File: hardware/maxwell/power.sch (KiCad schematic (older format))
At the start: 30 parts

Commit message: Adding finalized PCB layout.
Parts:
- removed C?: 100u, symbol CP
- added C17, C21: 15, fruchti/fruchtilib/mod/rcl.pretty:CP_13mm_200, symbol CP
- C15: renamed from C?; value ?500u -> 100u; footprint (none) -> xesscorp/xess.pretty:xess-ECAP-SMT-6.3MM
- C16, C18, C20: renamed from C?; footprint (none) -> coddingtonbear/coddingtonbear.pretty:0805_Milling
- C19: renamed from C?; value ?500u -> 220u; footprint (none) -> xesscorp/xess.pretty:xess-ECAP-SMT-6.3MM
- D1, D5, D6: renamed from D?; footprint (none) -> mcous/kicad-lib/footprints/diode.pretty:DO-214AC
- D2, D3: renamed from D?; value 25V -> 20; footprint (none) -> Tinkerforge/kicad-libraries:SOD523
- D4: renamed from D?; footprint (none) -> ep092/library_toni.pretty:SO-4
- J7, J9: renamed from J?; footprint (none) -> ChristianLerche/LercheTech_KiCAD/LercheTech.pretty:Lerche_2P_2.54mm_Terminal
- J8: renamed from J?; footprint (none) -> coddingtonbear/coddingtonbear.pretty:UJ2-MIBH-4-SMT
- R14, R15, R16, R17, R18, R19, R20, R21, R22, R23, R24: renamed from R?; footprint (none) -> coddingtonbear/coddingtonbear.pretty:0805_Milling
- U*1: renamed from U*?; footprint (none) -> apexelectrix/apex-smd.pretty:SOT-23-5
- U10: renamed from U?; footprint TO_SOT_Packages_THT:TO-220-4_Vertical -> KiCad/TO_SOT_Packages_THT.pretty:TO-220-5_Pentawatt_Multiwatt-5_Horizontal_StaggeredType2
- U8: renamed from U?; footprint Housings_SSOP:MFSOP6-4_4.4x3.6mm_Pitch1.27mm -> Tinkerforge/kicad-libraries:SO-4
- U9: renamed from U?; footprint (none) -> coddingtonbear/coddingtonbear.pretty:BOOST_LM2596_3A
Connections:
- net labels removed: Earth
- wire segments 60 -> 63

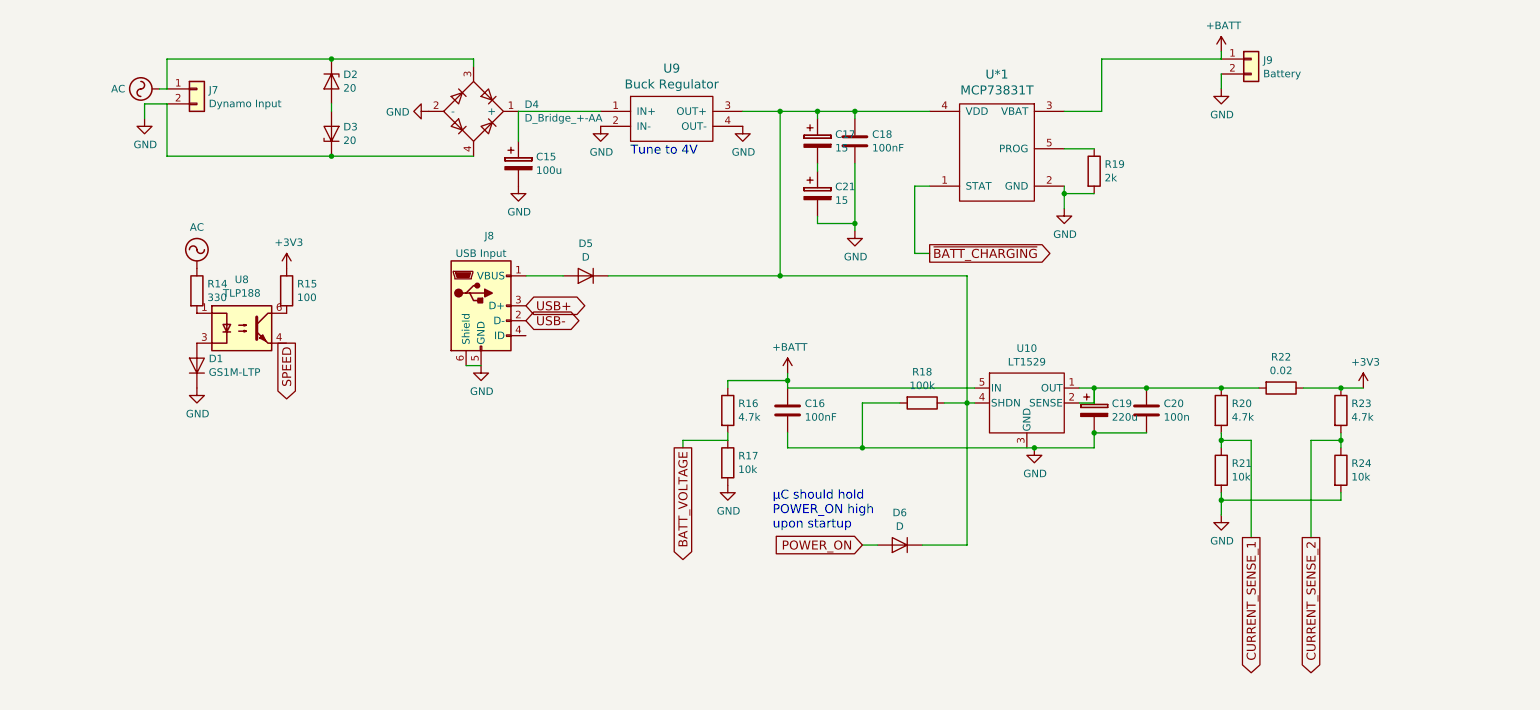
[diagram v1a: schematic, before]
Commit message: Updating schematic to add reverse polarity protection, higher-current diodes for zener limiting, and a low-side n-channel mosfet for enabling/disabling devices receiving direct battery power (limiting that quiescent current as much as possible).
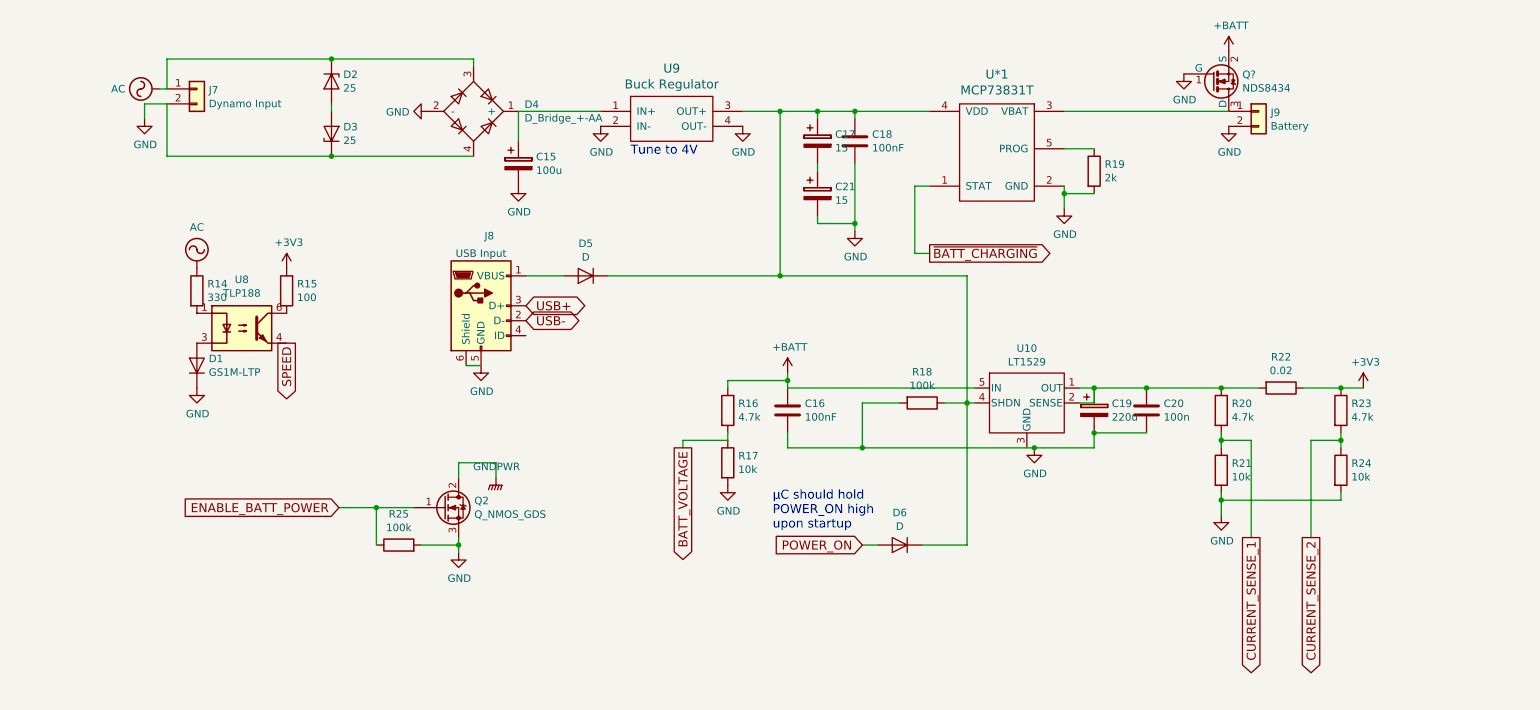
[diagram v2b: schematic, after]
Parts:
- added Q2: Q_NMOS_GDS, fruchti/fruchtilib/mod/to.pretty:TO220, symbol Q_NMOS_GDS
- added Q?: NDS8434, SOIC, symbol NDS8434
- added R25: 100k, coddingtonbear/coddingtonbear.pretty:0805_Milling, symbol R
- D2, D3: value 20 -> 25; footprint Tinkerforge/kicad-libraries:SOD523 -> coddingtonbear/coddingtonbear.pretty:DIODE-VERTICAL
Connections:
- net +BATT: now also Q?.2 (S); no longer J9.1 (Pin_1), U*1.3 (VBAT)
- net GND: now also Q2.3 (S), Q?.1 (G), R25.2
- new net: J9.1 (Pin_1), Q?.3 (D), U*1.3 (VBAT)
- new net ENABLE_BATT_POWER: Q2.1 (G), R25.1
- new net GNDPWR: Q2.2 (D)
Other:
- moved on the sheet: J9
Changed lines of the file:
@@
 P 2400 1050
 F 0 "D2" V 2354 1129 50  0000 L CNN
-F 1 "20" V 2445 1129 50  0000 L CNN
-F 2 "Tinkerforge/kicad-libraries:SOD523" H 2400 1050 50  0001 C CNN
+F 1 "25" V 2445 1129 50  0000 L CNN
+F 2 "coddingtonbear/coddingtonbear.pretty:DIODE-VERTICAL" H 2400 1050 50  0001 C CNN
 F 3 "" H 2400 1050 50  0001 C CNN
 	1    2400 1050
@@
 P 2400 1400
 F 0 "D3" V 2446 1321 50  0000 R CNN
-F 1 "20" V 2355 1321 50  0000 R CNN
-F 2 "Tinkerforge/kicad-libraries:SOD523" H 2400 1400 50  0001 C CNN
+F 1 "25" V 2355 1321 50  0000 R CNN
+F 2 "coddingtonbear/coddingtonbear.pretty:DIODE-VERTICAL" H 2400 1400 50  0001 C CNN
 F 3 "" H 2400 1400 50  0001 C CNN
 	1    2400 1400
@@
 L Conn_01x02 J9
 U 1 1 5A21040E
-P 8550 900
-F 0 "J9" H 8630 892 50  0000 L CNN
-F 1 "Battery" H 8630 801 50  0000 L CNN
-F 2 "ChristianLerche/LercheTech_KiCAD/LercheTech.pretty:Lerche_2P_2.54mm_Terminal" H 8550 900 50  0001 C CNN
-F 3 "" H 8550 900 50  0001 C CNN
-	1    8550 900
+P 8600 1250
+F 0 "J9" H 8680 1242 50  0000 L CNN
+F 1 "Battery" H 8680 1151 50  0000 L CNN
+F 2 "ChristianLerche/LercheTech_KiCAD/LercheTech.pretty:Lerche_2P_2.54mm_Terminal" H 8600 1250 50  0001 C CNN
+F 3 "" H 8600 1250 50  0001 C CNN
+	1    8600 1250
 	1    0    0    -1
 $EndComp
@@
 L GND #PWR042
 U 1 1 5A210626
-P 8350 1100
-F 0 "#PWR042" H 8350 850 50  0001 C CNN
-F 1 "GND" H 8355 927 50  0000 C CNN
-F 2 "" H 8350 1100 50  0001 C CNN
-F 3 "" H 8350 1100 50  0001 C CNN
-	1    8350 1100
+P 8400 1350
+F 0 "#PWR042" H 8400 1100 50  0001 C CNN
+F 1 "GND" H 8405 1177 50  0000 C CNN
+F 2 "" H 8400 1350 50  0001 C CNN
+F 3 "" H 8400 1350 50  0001 C CNN
+	1    8400 1350
 	1    0    0    -1
 $EndComp
@@
 L +BATT #PWR043
 U 1 1 5A210C7A
-P 8350 850
-F 0 "#PWR043" H 8350 700 50  0001 C CNN
-F 1 "+BATT" H 8365 1023 50  0000 C CNN
-F 2 "" H 8350 850 50  0001 C CNN
-F 3 "" H 8350 850 50  0001 C CNN
-	1    8350 850
+P 8400 850
+F 0 "#PWR043" H 8400 700 50  0001 C CNN
+F 1 "+BATT" H 8415 1023 50  0000 C CNN
+F 2 "" H 8400 850 50  0001 C CNN
+F 3 "" H 8400 850 50  0001 C CNN
+	1    8400 850
 	1    0    0    -1
 $EndComp
@@
 	7300 1750 7300 1900
 Wire Wire Line
-	7550 900  8350 900
-Wire Wire Line
-	8350 1100 8350 1000
-Wire Wire Line
 	7500 1800 7300 1800
 Connection ~ 7300 1800
 Wire Wire Line
 	7500 1500 7300 1500
-Wire Wire Line
-	8350 900  8350 850
 Wire Wire Line
 	5150 1250 6400 1250
@@
 $EndComp
 Wire Wire Line
-	7300 1250 7550 1250
-Wire Wire Line
-	7550 1250 7550 900
+	7300 1250 8400 1250
 Wire Wire Line
 	5650 1600 5650 1650
@@
 	1    0    0    -1
 $EndComp
+$Comp
+L Q_NMOS_GDS Q2
+U 1 1 5A257F55
+P 3150 3900
+F 0 "Q2" H 3355 3946 50  0000 L CNN
+F 1 "Q_NMOS_GDS" H 3355 3855 50  0000 L CNN
+F 2 "fruchti/fruchtilib/mod/to.pretty:TO220" H 3350 4000 50  0001 C CNN
+F 3 "" H 3150 3900 50  0001 C CNN
+	1    3150 3900
+	1    0    0    -1
+$EndComp
+$Comp
+L GNDPWR #PWR049
+U 1 1 5A25809F
+P 3500 3700
+F 0 "#PWR049" H 3500 3500 50  0001 C CNN
+F 1 "GNDPWR" H 3504 3774 50  0000 C CNN
+F 2 "" H 3500 3650 50  0001 C CNN
+F 3 "" H 3500 3650 50  0001 C CNN
+	1    3500 3700
+	1    0    0    -1
+$EndComp
+$Comp
+L GND #PWR050
+U 1 1 5A2580F1
+P 3250 4200
+F 0 "#PWR050" H 3250 3950 50  0001 C CNN
+F 1 "GND" H 3255 4027 50  0000 C CNN
+F 2 "" H 3250 4200 50  0001 C CNN
+F 3 "" H 3250 4200 50  0001 C CNN
+	1    3250 4200
+	1    0    0    -1
+$EndComp
+Wire Wire Line
+	3250 3700 3250 3600
+Wire Wire Line
+	3250 3600 3500 3600
+Wire Wire Line
+	3500 3600 3500 3700
+Wire Wire Line
+	3250 4200 3250 4100
+$Comp
+L R R25
+U 1 1 5A25869F
+P 2850 4150
+F 0 "R25" V 3057 4150 50  0000 C CNN
+F 1 "100k" V 2966 4150 50  0000 C CNN
+F 2 "coddingtonbear/coddingtonbear.pretty:0805_Milling" V 2780 4150 50  0001 C CNN
+F 3 "" H 2850 4150 50  0001 C CNN
+	1    2850 4150
+	0    -1   -1   0
+$EndComp
+Wire Wire Line
+	2450 3900 2950 3900
+Connection ~ 2700 3900
+Wire Wire Line
+	3000 4150 3250 4150
+Connection ~ 3250 4150
+Wire Wire Line
+	2700 4150 2700 3900
+Text GLabel 2450 3900 0    60   Input ~ 0
+ENABLE_BATT_POWER
+$Comp
+L NDS8434 Q?
+U 1 1 5A25C576
+P 8300 1050
+F 0 "Q?" H 8491 1004 50  0000 L CNN
+F 1 "NDS8434" H 8491 1095 50  0000 L CNN
+F 2 "SOIC" H 8500 950 50  0001 L CIN
+F 3 "" H 8300 1050 50  0000 L CNN
+	1    8300 1050
+	1    0    0    1
+$EndComp
+$Comp
+L GND #PWR?
+U 1 1 5A25CAAF
+P 8100 1000
+F 0 "#PWR?" H 8100 750 50  0001 C CNN
+F 1 "GND" H 8105 827 50  0000 C CNN
+F 2 "" H 8100 1000 50  0001 C CNN
+F 3 "" H 8100 1000 50  0001 C CNN
+	1    8100 1000
+	1    0    0    -1
+$EndComp

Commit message: More minor changes and fixes.
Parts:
- removed C21: 15, fruchti/fruchtilib/mod/rcl.pretty:CP_13mm_200, symbol CP
- added R?: 1.5k, coddingtonbear/coddingtonbear.pretty:0805_Milling, symbol R
- C17: value 15 -> 0.1
- Q3: renamed from Q?; footprint SOIC -> coddingtonbear/coddingtonbear.pretty:NDS8434
- R15: value 100 -> 330
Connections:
- net +3V3: now also U8.6; no longer R15.1
- net AC: now also U8.1; no longer R14.1
- net GND: now also C17.2; no longer D1.1 (K), D3.1 (K), D4.4, J7.2 (Pin_2)
- net SPEED: now also R15.2; no longer U8.4
- net at R14.2: now also D1.2 (A); no longer U8.1
- net at U8.3: now also R14.1; no longer D1.2 (A)
- net at C17.1, C18.2, D5.1 (K)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: now also R?.2; no longer D6.1 (K), R18.1, U10.4 (SHDN)
- new net: R15.1, U8.4
- new net: D6.1 (K), R18.1, R?.1, U10.4 (SHDN)
- new net AC_NEUTRAL: D1.1 (K), D3.1 (K), D4.4, J7.2 (Pin_2)
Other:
- moved on the sheet: D1, R14, R15
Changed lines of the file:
@@
 L D D1
 U 1 1 5A1FF263
-P 1500 2950
-F 0 "D1" V 1546 2871 50  0000 R CNN
-F 1 "GS1M-LTP" V 1455 2871 50  0000 R CNN
-F 2 "mcous/kicad-lib/footprints/diode.pretty:DO-214AC" H 1500 2950 50  0001 C CNN
-F 3 "" H 1500 2950 50  0001 C CNN
-	1    1500 2950
+P 1500 3250
+F 0 "D1" V 1546 3171 50  0000 R CNN
+F 1 "GS1M-LTP" V 1455 3171 50  0000 R CNN
+F 2 "mcous/kicad-lib/footprints/diode.pretty:DO-214AC" H 1500 3250 50  0001 C CNN
+F 3 "" H 1500 3250 50  0001 C CNN
+	1    1500 3250
 	0    -1   -1   0
 $EndComp
@@
 L AC #PWR031
 U 1 1 5A1FF26A
-P 1500 2300
-F 0 "#PWR031" H 1500 2200 50  0001 C CNN
-F 1 "AC" H 1500 2575 50  0000 C CNN
-F 2 "" H 1500 2300 50  0001 C CNN
-F 3 "" H 1500 2300 50  0001 C CNN
-	1    1500 2300
+P 1500 2600
+F 0 "#PWR031" H 1500 2500 50  0001 C CNN
+F 1 "AC" H 1500 2875 50  0000 C CNN
+F 2 "" H 1500 2600 50  0001 C CNN
+F 3 "" H 1500 2600 50  0001 C CNN
+	1    1500 2600
 	1    0    0    -1
 $EndComp
@@
 L R R15
 U 1 1 5A1FF270
-P 2100 2450
-F 0 "R15" H 2170 2496 50  0000 L CNN
-F 1 "100" H 2170 2405 50  0000 L CNN
-F 2 "coddingtonbear/coddingtonbear.pretty:0805_Milling" V 2030 2450 50  0001 C CNN
-F 3 "" H 2100 2450 50  0001 C CNN
-	1    2100 2450
+P 2100 2950
+F 0 "R15" H 2170 2996 50  0000 L CNN
+F 1 "330" H 2170 2905 50  0000 L CNN
+F 2 "coddingtonbear/coddingtonbear.pretty:0805_Milling" V 2030 2950 50  0001 C CNN
+F 3 "" H 2100 2950 50  0001 C CNN
+	1    2100 2950
 	1    0    0    -1
 $EndComp
@@
 L +3V3 #PWR032
 U 1 1 5A1FF277
-P 2100 2300
-F 0 "#PWR032" H 2100 2150 50  0001 C CNN
-F 1 "+3V3" H 2115 2473 50  0000 C CNN
-F 2 "" H 2100 2300 50  0001 C CNN
-F 3 "" H 2100 2300 50  0001 C CNN
-	1    2100 2300
-	1    0    0    -1
-$EndComp
-Text GLabel 2100 2800 3    60   Output ~ 0
+P 2100 2600
+F 0 "#PWR032" H 2100 2450 50  0001 C CNN
+F 1 "+3V3" H 2115 2773 50  0000 C CNN
+F 2 "" H 2100 2600 50  0001 C CNN
+F 3 "" H 2100 2600 50  0001 C CNN
+	1    2100 2600
+	1    0    0    -1
+$EndComp
+Text GLabel 2100 3100 3    60   Output ~ 0
 SPEED
 $Comp
@@
 L R R14
 U 1 1 5A1FF297
-P 1500 2450
-F 0 "R14" H 1570 2496 50  0000 L CNN
-F 1 "330" H 1570 2405 50  0000 L CNN
-F 2 "coddingtonbear/coddingtonbear.pretty:0805_Milling" V 1430 2450 50  0001 C CNN
-F 3 "" H 1500 2450 50  0001 C CNN
-	1    1500 2450
+P 1500 2950
+F 0 "R14" H 1570 2996 50  0000 L CNN
+F 1 "330" H 1570 2905 50  0000 L CNN
+F 2 "coddingtonbear/coddingtonbear.pretty:0805_Milling" V 1430 2950 50  0001 C CNN
+F 3 "" H 1500 2950 50  0001 C CNN
+	1    1500 2950
 	1    0    0    -1
 $EndComp
@@
 $EndComp
 $Comp
-L GND #PWR046
-U 1 1 5A224AB0
-P 1150 1300
-F 0 "#PWR046" H 1150 1050 50  0001 C CNN
-F 1 "GND" H 1155 1127 50  0000 C CNN
-F 2 "" H 1150 1300 50  0001 C CNN
-F 3 "" H 1150 1300 50  0001 C CNN
-	1    1150 1300
-	1    0    0    -1
-$EndComp
-$Comp
 L R R18
 U 1 1 5A2253E0
@@
 	7850 3400 7500 3400
 Wire Wire Line
-	7500 3400 7500 3500
+	7500 3500 7500 3400
 Connection ~ 7100 3500
 Wire Wire Line
@@
 	5400 2350 5400 1250
 Wire Wire Line
-	7500 3500 5450 3500
+	5450 3500 7500 3500
 Wire Wire Line
 	5900 1300 5900 1250
@@
 Connection ~ 5650 1250
 Wire Wire Line
-	1300 1200 1150 1200
-Wire Wire Line
-	1150 1200 1150 1300
-Wire Wire Line
-	6700 3100 5450 3100
-Wire Wire Line
-	5450 3100 5450 3000
+	5450 3100 6700 3100
+Wire Wire Line
+	5450 3000 5450 3100
 Wire Wire Line
 	5450 3500 5450 3400
@@
 	4250 2350 6650 2350
 Wire Wire Line
-	6650 2350 6650 4150
+	6650 2650 6650 4150
 Connection ~ 5400 2350
 Wire Wire Line
@@
 	7300 1250 8400 1250
 Wire Wire Line
-	5650 1600 5650 1650
-Wire Wire Line
-	5650 1950 5650 2000
+	5650 1600 5650 2000
 Wire Wire Line
 	5650 2000 5900 2000
@@
 P 5650 1450
 F 0 "C17" H 5768 1496 50  0000 L CNN
-F 1 "15" H 5768 1405 50  0000 L CNN
+F 1 "0.1" H 5768 1405 50  0000 L CNN
 F 2 "fruchti/fruchtilib/mod/rcl.pretty:CP_13mm_200" H 5688 1300 50  0001 C CNN
 F 3 "" H 5650 1450 50  0001 C CNN
@@
 	1    0    0    -1
 $EndComp
-$Comp
-L CP C21
-U 1 1 5A24B12E
-P 5650 1800
-F 0 "C21" H 5768 1846 50  0000 L CNN
-F 1 "15" H 5768 1755 50  0000 L CNN
-F 2 "fruchti/fruchtilib/mod/rcl.pretty:CP_13mm_200" H 5688 1650 50  0001 C CNN
-F 3 "" H 5650 1800 50  0001 C CNN
-	1    5650 1800
-	1    0    0    -1
-$EndComp
 Wire Wire Line
 	1250 1100 1300 1100
@@
 Wire Wire Line
 	1300 1550 1300 1200
-$Comp
-L GND #PWR034
-U 1 1 5A24CA3D
-P 1500 3100
-F 0 "#PWR034" H 1500 2850 50  0001 C CNN
-F 1 "GND" H 1505 2927 50  0000 C CNN
-F 2 "" H 1500 3100 50  0001 C CNN
-F 3 "" H 1500 3100 50  0001 C CNN
-	1    1500 3100
-	1    0    0    -1
-$EndComp
 $Comp
 L Q_NMOS_GDS Q2
@@
 	3500 3600 3500 3700
 Wire Wire Line
-	3250 4200 3250 4100
+	3250 4100 3250 4200
 $Comp
 L R R25
@@
 ENABLE_BATT_POWER
 $Comp
-L NDS8434 Q?
+L NDS8434 Q3
 U 1 1 5A25C576
 P 8300 1050
-F 0 "Q?" H 8491 1004 50  0000 L CNN
+F 0 "Q3" H 8491 1004 50  0000 L CNN
 F 1 "NDS8434" H 8491 1095 50  0000 L CNN
-F 2 "SOIC" H 8500 950 50  0001 L CIN
+F 2 "coddingtonbear/coddingtonbear.pretty:NDS8434" H 8500 950 50  0001 L CIN
 F 3 "" H 8300 1050 50  0000 L CNN
 	1    8300 1050
@@
 $EndComp
 $Comp
-L GND #PWR?
+L GND #PWR051
 U 1 1 5A25CAAF
 P 8100 1000
-F 0 "#PWR?" H 8100 750 50  0001 C CNN
+F 0 "#PWR051" H 8100 750 50  0001 C CNN
 F 1 "GND" H 8105 827 50  0000 C CNN
 F 2 "" H 8100 1000 50  0001 C CNN
@@
 	1    0    0    -1
 $EndComp
+Text GLabel 1300 1200 0    60   Input ~ 0
+AC_NEUTRAL
+Text GLabel 1350 3500 0    60   Input ~ 0
+AC_NEUTRAL
+Wire Wire Line
+	1500 3400 1500 3500
+Wire Wire Line
+	1500 3500 1350 3500
+$Comp
+L R R?
+U 1 1 5A26A72F
+P 6650 2500
+F 0 "R?" V 6443 2500 50  0000 C CNN
+F 1 "1.5k" V 6534 2500 50  0000 C CNN
+F 2 "coddingtonbear/coddingtonbear.pretty:0805_Milling" V 6580 2500 50  0001 C CNN
+F 3 "" H 6650 2500 50  0001 C CNN
+	1    6650 2500
+	-1   0    0    1
+$EndComp
 $EndSCHEMATC

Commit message: More fixes, additions, improvements.
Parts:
- added Q4: Q_NMOS_GSD, adamgreig/agg-kicad/agg.pretty:SOT-23, symbol Q_NMOS_GSD
- added R34, R36: 10k, coddingtonbear/coddingtonbear.pretty:0805_Milling, symbol R
- added R35: 2k, coddingtonbear/coddingtonbear.pretty:0805_Milling, symbol R
- U10: footprint KiCad/TO_SOT_Packages_THT.pretty:TO-220-5_Pentawatt_Multiwatt-5_Horizontal_StaggeredType2 -> KiCad/TO_SOT_Packages_THT.pretty:TO-220-5_Pentawatt_Multiwatt-5_Vertical_StaggeredType2
- gave numbers to parts that had none: 1
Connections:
- net GND: now also Q4.2 (S), R35.2, R36.1; no longer R19.2
- net at C15.1, D4.1 (+), U9.1 (IN+): now also R34.1
- new net: Q4.3 (D), R19.2
- new net BATT_CHARGE_ENABLE: Q4.1 (G), R36.2
- new net DYNAMO_VOLTAGE: R34.2, R35.1
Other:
- moved on the sheet: R19
